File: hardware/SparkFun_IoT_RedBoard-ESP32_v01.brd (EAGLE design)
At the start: 68.6 x 58.4 mm, 214 parts, among them J1 5.5x2.1mm Barrel, J13 QWIIC_RIGHT_ANGLE, J15 MICRO-SD-PUSH-PUSH-EXT-PIN, J2 USB C, J3 USB_SOLDER_PADS, J5 M10NO_SILK, Q1 MBT3904DW1T1, Q11 20V/4.2A/52mΩ/1.4W, Q13 20V/4.2A/52mΩ/1.4W, Q3 20V/4.2A/52mΩ/1.4W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

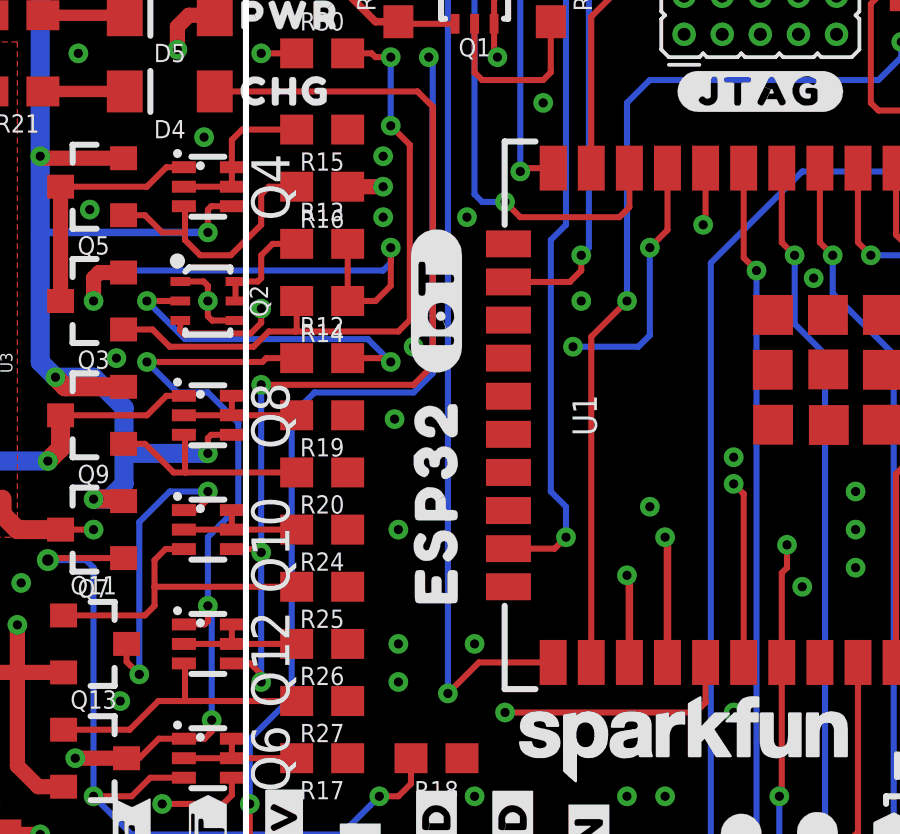
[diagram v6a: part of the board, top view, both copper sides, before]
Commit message: Add addressable status LED
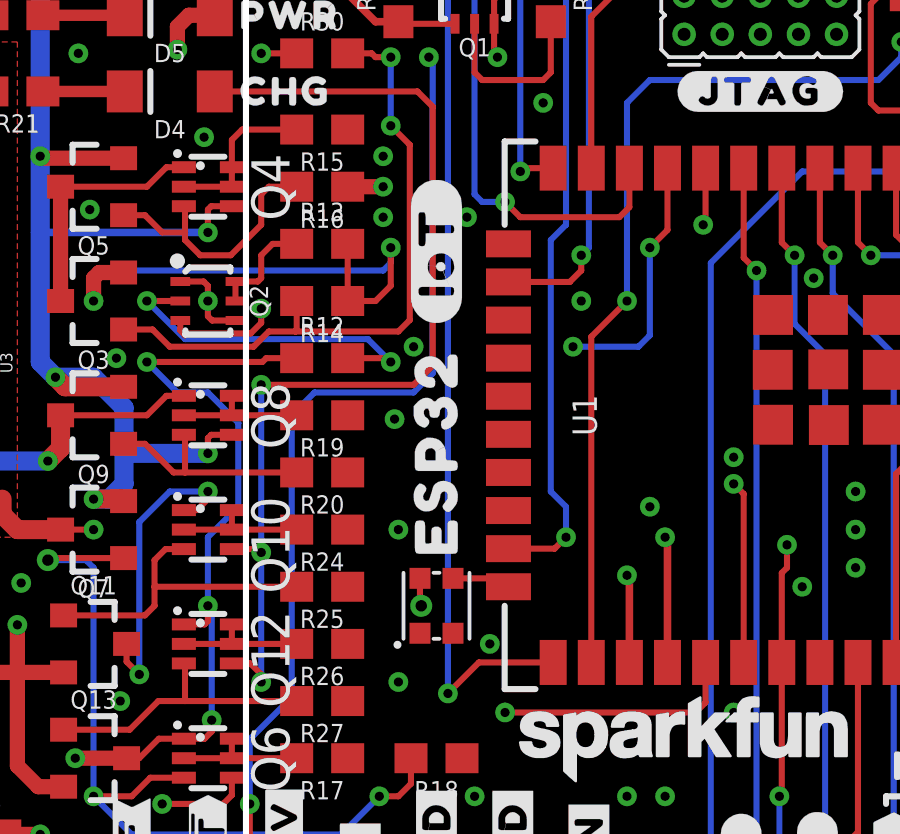
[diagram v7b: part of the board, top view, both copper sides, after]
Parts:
- added D7: WS2812_2020, SparkFun-LED:WS2812-2020
- moved U$100 1.65 mm to (40.6, 29.6)
- moved U$48 1.65 mm to (40.6, 18.4)
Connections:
- net 3.3V: now also D7.VCC
- net ESP32_GPIO2: now also D7.DI
- net GND: now also D7.GND
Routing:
- net ESP32_GPIO2: track 0.00 -> 1.97 mm
- net 3.3V: track 53.3 -> 54.2 mm, vias 12 -> 13
- net GND: vias 146 -> 145
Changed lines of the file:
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@@
 <element name="U$45" library="output-ESP32" package="#BATT#1848" value="" x="21.59" y="14.859" smashed="yes" rot="MR0"/>
 <element name="U$46" library="output-ESP32" package="#JTAG#1847" value="" x="51.435" y="34.925" smashed="yes" rot="MR0"/>
-<element name="U$48" library="output-ESP32" package="ESP321855" value="" x="40.64" y="16.764" smashed="yes" rot="R90"/>
+<element name="U$48" library="output-ESP32" package="ESP321855" value="" x="40.64" y="18.415" smashed="yes" rot="R90"/>
 <element name="U$49" library="output-ESP32" package="7#15V32321861" value="" x="11.43" y="3.81" smashed="yes" rot="R90"/>
 <element name="U$50" library="output-ESP32" package="#39#A3#321862" value="" x="60.96" y="1.778" smashed="yes" rot="MR90"/>
@@
 <element name="U$95" library="output-ESP32" package="TP1321868" value="" x="50.8" y="45.212" smashed="yes" rot="MR90"/>
 <element name="U$98" library="SparkFun-Aesthetics" package="REDBOARD_LOGO" value="" x="45.72" y="22.86" smashed="yes" rot="MR0"/>
-<element name="U$100" library="output-ESP32" package="#IOT#132321869" value="" x="40.64" y="27.94" smashed="yes" rot="R90"/>
+<element name="U$100" library="output-ESP32" package="#IOT#132321869" value="" x="40.64" y="29.591" smashed="yes" rot="R90"/>
 <element name="U$93" library="output-ESP32" package="ESP32321856" value="" x="40.005" y="21.463" smashed="yes" rot="MR0"/>
 <element name="U$47" library="output-ESP32" package="#IOT#132321874" value="" x="26.162" y="32.639" smashed="yes" rot="MR0"/>
@@
 <element name="U$11" library="output" package="#MEAS#0" value="" x="46.355" y="46.609" smashed="yes" rot="MR0"/>
 <element name="U$64" library="output" package="#BYP#0" value="" x="45.085" y="41.783" smashed="yes" rot="MR0"/>
+<element name="D7" library="SparkFun-LED" package="WS2812-2020" value="WS2812_2020" x="40.64" y="17.78" smashed="yes" rot="R270">
+<attribute name="PROD_ID" value="DIO-15591" x="40.64" y="17.78" size="1.778" layer="27" font="vector" ratio="15" rot="R270" display="off"/>
+</element>
 </elements>
 <signals>
@@
 <via x="46.99" y="11.43" extent="1-16" drill="0.3048"/>
 <via x="39.37" y="15.24" extent="1-16" drill="0.3048"/>
-<via x="39.37" y="16.51" extent="1-16" drill="0.3048"/>
-<via x="41.91" y="16.51" extent="1-16" drill="0.3048"/>
+<via x="42.418" y="16.51" extent="1-16" drill="0.3048"/>
 <via x="39.37" y="20.32" extent="1-16" drill="0.3048"/>
 <via x="16.51" y="19.05" extent="1-16" drill="0.3048"/>
@@
 <contactref element="C18" pad="2"/>
 <via x="42.926" y="47.879" extent="1-16" drill="0.3048"/>
+<contactref element="D7" pad="GND"/>
 </signal>
 <signal name="VIN" class="1">
@@
 <wire x1="32.385" y1="37.465" x2="33.25" y2="37.465" width="0.508" layer="1"/>
 <wire x1="32.004" y1="37.084" x2="32.385" y2="37.465" width="0.508" layer="1"/>
+<contactref element="D7" pad="VCC"/>
+<wire x1="40.09" y1="18.695" x2="40.09" y2="17.822" width="0.2032" layer="1"/>
+<wire x1="40.09" y1="17.822" x2="40.132" y2="17.78" width="0.2032" layer="1"/>
+<via x="40.132" y="17.78" extent="1-16" drill="0.381"/>
 </signal>
 <signal name="ESP32_SCL">
@@
 <signal name="ESP32_GPIO2">
 <contactref element="U1" pad="24"/>
+<contactref element="D7" pad="DI"/>
+<wire x1="43.04" y1="18.415" x2="42.76" y2="18.695" width="0.2032" layer="1"/>
+<wire x1="42.76" y1="18.695" x2="41.19" y2="18.695" width="0.2032" layer="1"/>
 </signal>
 <signal name="ESP32_GPIO4">
